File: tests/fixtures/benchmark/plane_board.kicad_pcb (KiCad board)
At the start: 2 copper layers, 50 x 38 mm, 12 parts, among them J1 PWR, J2 IO, J3 AUX, U1 SENSOR-HUB, U2 LDO

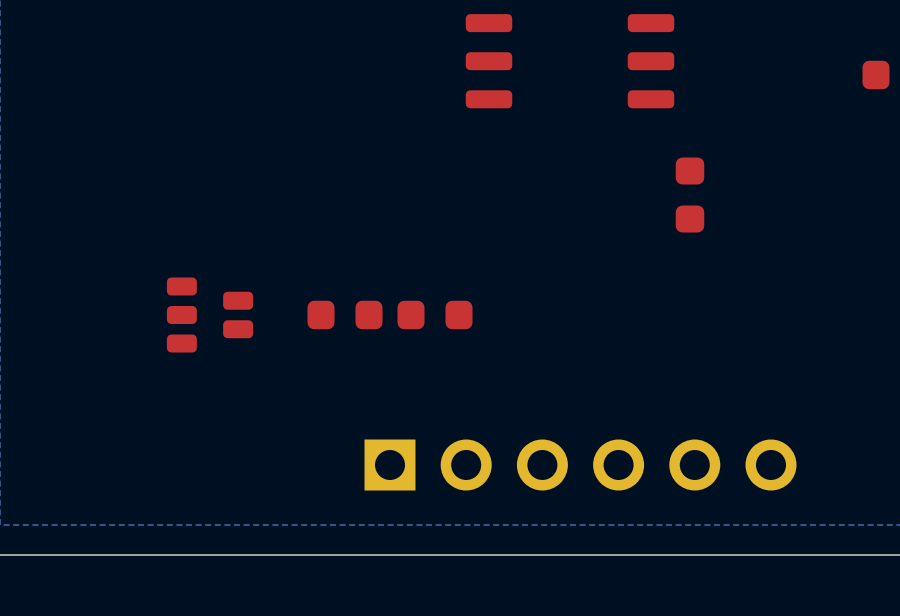
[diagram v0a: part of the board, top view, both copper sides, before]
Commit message: fix(benchmark): two parts in the same place, on a fixture and on two others
plane_board.kicad_pcb put C1 and C2 3mm apart. An 0603 courtyard is about 3mm
wide once the IPC excess is added either side, so they touched at exactly
0.00mm against 0.25mm required. That was mine, four fires old, reported at the
time and not fixed. It is fixed at the generator rather than in the file, so
make_plane_board.py and the board it writes agree.

Asked of every fixture before touching anything, which nothing had ever done:

  led_blink.kicad_pcb: 0
  multi_ic.kicad_pcb: 26
  plane_board.kicad_pcb: 1
  qfp_fanout.kicad_pcb: 0
  shift_driver.kicad_pcb: 0
  stm32_breakout.kicad_pcb: 2

A courtyard is the room a part needs to be placed and soldered, so two that
overlap are two parts that cannot both go on the board.
no_fixture_asks_for_two_parts_in_the_same_place holds each board against a
known count, the way the off-board-pad check does. The 26 and the 2 predate
this by a long way and repairing either moves its ratchet and every table
drawn from it, so they are recorded rather than tolerated in silence.

The previous tracker entry said this moves no ratchet because a courtyard
overlap is a placement fault rather than a routing one. That was wrong.
Moving one capacitor 1mm moved the routing:

  before: 210 routes, 40 violations, 18 shorts
  after:  181 routes, 28 violations, 13 shorts

  plane_board: 181 routes, 28 violations against 37, 13 shorts against 18,
               0 unrouted

The ratchet is re-measured and tightened, 49/23 -> 37/18. The band is carried
over from the board before the move and the comment says so: a 1mm move does
not change how sensitive a board is to the via price, but it was not
re-measured, and the ratchet only tightens either way.

Workspace: 107 suites ok, 0 failed. Gate:
  [1/8] fmt OK [2/8] clippy OK [3/8] test OK [4/8] eslint OK [5/8] vitest OK
  [6/8] playwright OK [7/8] benchmark OK [8/8] jscpd OK
  === All stages passed ===
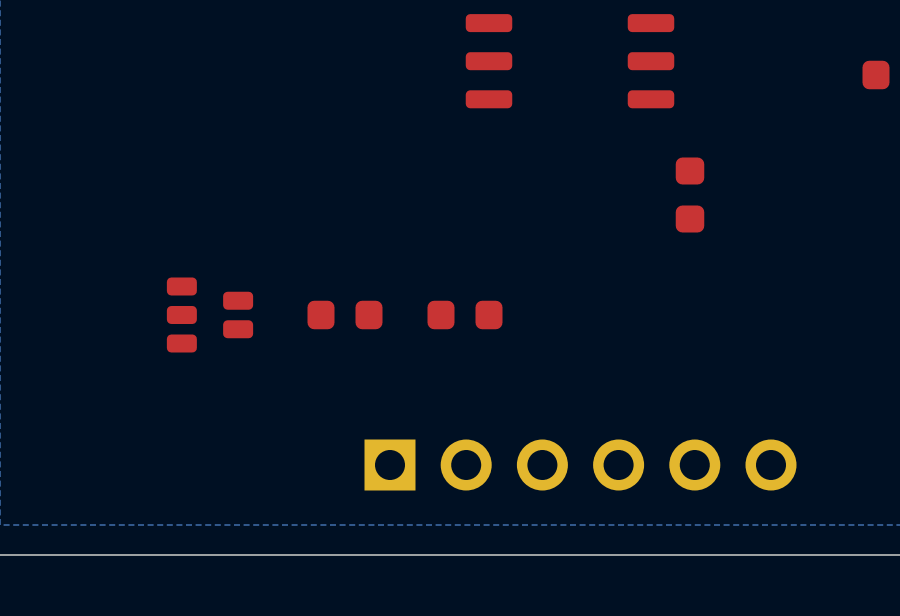
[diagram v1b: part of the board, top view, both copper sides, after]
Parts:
- moved C2 1.00 mm to (116.5, 90.0)
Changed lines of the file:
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@@
   (footprint "Capacitor_SMD:C_0603_1608Metric"
     (layer "F.Cu")
-    (at 115.500 90.000)
+    (at 116.500 90.000)
     (property "Reference" "C2")
     (property "Value" "100nF")
